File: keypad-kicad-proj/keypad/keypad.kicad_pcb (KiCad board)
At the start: 2 copper layers, 160 x 125 mm, 103 parts, among them J1 Screw_Terminal_01x02, J2 USB4105-GF-A, J3 USB4105-GF-A, J4 Micro_SD_Card_Det_Hirose_DM3AT, Q1 BC817, Q2 BC817, Q3 IRF9393TRPBF, SW1 RotaryEncoder, SW2 RotaryEncoder, SW25 SW_RST, SW26 Cherry_MX, SW27 Cherry_MX, SW28 Cherry_MX, SW32 Cherry_MX, SW33 Cherry_MX, SW34 Cherry_MX, SW38 Cherry_MX, SW39 Cherry_MX, SW40 Cherry_MX, SW44 Cherry_MX, SW45 Cherry_MX, SW46 Cherry_MX, U1 ESP32-S3-WROOM-1, U10 SK6812MINI-E, U11 SK6812MINI-E, U12 SK6812MINI-E, U13 SK6812MINI-E, U14 SK6812MINI-E, U2 TLV75901PDRVT, U27 SK6812MINI-E, U3 CP2102N-A01-GQFN24, U4 SK6812MINI-E, U5 SK6812MINI-E, U6 SK6812MINI-E, U7 SK6812MINI-E, U8 SK6812MINI-E, U9 SK6812MINI-E

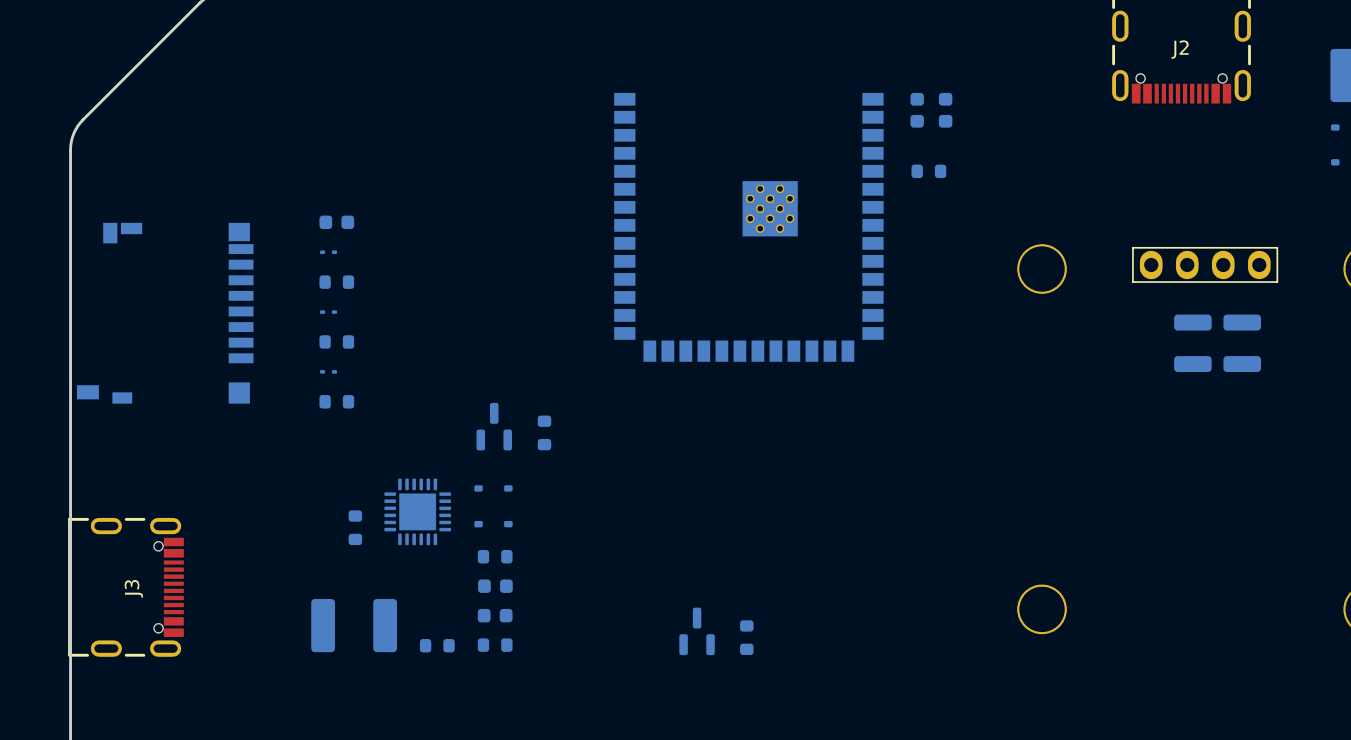
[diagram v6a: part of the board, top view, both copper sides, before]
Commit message: assigned different pins so it's easier for the layout
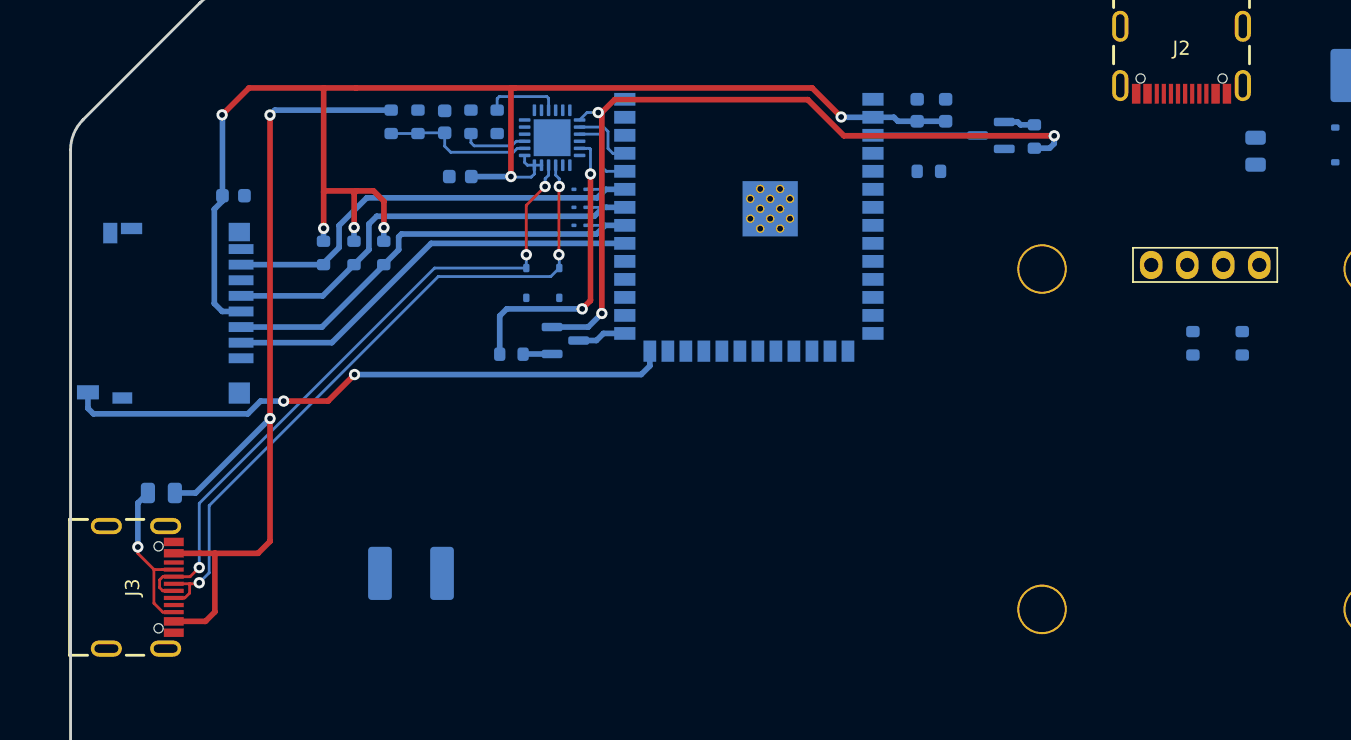
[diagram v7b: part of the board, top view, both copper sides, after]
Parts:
- added R22: 56k, Capacitor_SMD:C_0805_2012Metric, B.Cu at (55.9, 75.3)
- added R23: 56k, Capacitor_SMD:C_0805_2012Metric, B.Cu at (133.1, 51.2)
- R21, R6: footprint Resistor_SMD:R_1210_3225Metric -> Resistor_SMD:R_0603_1608Metric
- moved R10 40.7 mm to (117.5, 50.2), turned to -90 degrees
- moved Q1 40.6 mm to (114.4, 50.1), turned to 180 degrees
- moved R7 37.3 mm to (74.0, 49.1), turned to 90 degrees
- moved R5 37.1 mm to (72.1, 49.1), turned to -90 degrees
- moved C5 35.0 mm to (75.9, 49.1), turned to 90 degrees
- moved R9 30.7 mm to (77.7, 49.1), turned to 90 degrees
- moved R8 30.3 mm to (79.6, 49.1)
- moved C6 29.0 mm to (77.0, 53.0)
- moved U3 28.0 mm to (83.5, 50.3), turned to 90 degrees
- moved D25 20.5 mm to (85.4, 56.4), turned to 180 degrees
- moved D24 19.2 mm to (85.4, 55.2), turned to 180 degrees
- moved D23 18.3 mm to (85.4, 53.9), turned to 180 degrees
- moved D21 17.2 mm to (81.7, 60.5), turned to -90 degrees
- moved D19 15.2 mm to (84.0, 60.5), turned to -90 degrees
- moved R15 11.0 mm to (71.6, 58.4), turned to -90 degrees
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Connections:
- U1 pad 10: unconnected-(U1-IO17-Pad10) -> rotary_encoder_1B
- U1 pad 11: unconnected-(U1-IO18-Pad11) -> rotary_encoder_2B
- U1 pad 12: rotary_encoder_1A -> unconnected-(U1-IO8-Pad12)
- U1 pad 16: row_0 -> unconnected-(U1-IO46-Pad16)
- U1 pad 17: rotary_encoder_1B -> unconnected-(U1-IO9-Pad17)
- U1 pad 18: rotary_encoder_2A -> col_3
- U1 pad 19: rotary_encoder_2B -> col_2
- U1 pad 20: slide_potentiometer -> col_1
- U1 pad 22: col_1 -> row_2
- U1 pad 23: unconnected-(U1-IO21-Pad23) -> row_1
- U1 pad 24: unconnected-(U1-IO47-Pad24) -> row_0
- U1 pad 25: unconnected-(U1-IO48-Pad25) -> LED_strip
- U1 pad 28: row_1 -> unconnected-(U1-IO35-Pad28)
- U1 pad 29: row_2 -> unconnected-(U1-IO36-Pad29)
- U1 pad 5: LED_strip -> unconnected-(U1-IO5-Pad5)
- U1 pad 7: unconnected-(U1-IO7-Pad7) -> slide_potentiometer
- U1 pad 8: col_2 -> rotary_encoder_1A
- U1 pad 9: col_3 -> rotary_encoder_2A
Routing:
- net +3V3: track 0.00 -> 103.6 mm, vias 0 -> 6
- net USB-C_UART_VBUS: track 0.00 -> 62.1 mm, vias 0 -> 2
- net Net-(Q2-E): track 0.00 -> 55.0 mm, vias 0 -> 3
- net USB-C_UART_D+: track 0.00 -> 48.5 mm, vias 0 -> 3
- net USB-C_UART_D-: track 0.00 -> 47.2 mm, vias 0 -> 3
- net SD_DET: track 0.00 -> 43.3 mm, vias 0 -> 2
- net SD_CLK: track 0.00 -> 32.2 mm
- net SD_MOSI: track 0.00 -> 31.9 mm
- net SD_MISO: track 0.00 -> 31.7 mm
- net SD_CS: track 0.00 -> 30.0 mm
- net Net-(Q1-E): track 0.00 -> 21.0 mm, vias 0 -> 2
- net Net-(J3-CC1): track 0.00 -> 11.6 mm, vias 0 -> 1
- net Net-(U3-VBUS): track 0.00 -> 10.7 mm
- net RTS: track 0.00 -> 7.38 mm
- net UART_TX: track 0.00 -> 5.56 mm
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
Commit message: layout update
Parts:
- removed D1: LED, LED_SMD:LED_0805_2012Metric_Pad1.15x1.40mm_HandSolder
- removed R16: 2k, Resistor_SMD:R_0603_1608Metric
- moved D18 103.4 mm to (165.9, 34.6)
- moved R18 47.9 mm to (204.4, 99.8), turned to 0 degrees
- moved RV1 44.7 mm to (185.1, 101.3), turned to -90 degrees
- moved D27 44.3 mm to (199.3, 99.8), turned to 180 degrees
- moved R17 39.5 mm to (204.2, 95.6), turned to 0 degrees
- moved D26 35.3 mm to (199.3, 95.6), turned to 180 degrees
- moved R20 25.1 mm to (90.8, 68.8), turned to 0 degrees
- moved D17 17.0 mm to (155.2, 35.9)
- moved D16 16.1 mm to (145.7, 37.0), turned to 90 degrees
- moved Q3 15.9 mm to (199.3, 71.1)
- moved D22 15.6 mm to (200.7, 66.9)
- moved R2 14.8 mm to (192.9, 72.9), turned to 180 degrees
- moved R4 14.3 mm to (193.1, 70.9), turned to 0 degrees
- moved D15 12.8 mm to (140.6, 36.8), turned to 90 degrees
- moved R19 12.3 mm to (173.3, 76.1)
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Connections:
- U1 pad 10: rotary_encoder_1B -> rotary_encoder_2B
- U1 pad 11: rotary_encoder_2B -> rotary_encoder_2A
- U1 pad 16: unconnected-(U1-IO46-Pad16) -> rotary_encoder_1B
- U1 pad 17: unconnected-(U1-IO9-Pad17) -> rotary_encoder_1A
- U1 pad 4: indicator -> unconnected-(U1-IO4-Pad4)
- U1 pad 8: rotary_encoder_1A -> unconnected-(U1-IO15-Pad8)
- U1 pad 9: rotary_encoder_2A -> unconnected-(U1-IO16-Pad9)
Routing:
- net +5V: track 0.00 -> 371.0 mm, vias 0 -> 13
- net +3V3: track 103.6 -> 280.5 mm, vias 6 -> 9
- net row_2: track 0.00 -> 169.5 mm, vias 0 -> 3
- net row_1: track 0.00 -> 149.0 mm, vias 0 -> 1
- net rotary_encoder_1A: track 0.00 -> 138.0 mm
- net col_3: track 0.00 -> 133.6 mm
- net rotary_encoder_1B: track 0.00 -> 130.3 mm
- net row_0: track 0.00 -> 125.6 mm
- net slide_potentiometer: track 0.00 -> 120.9 mm, vias 0 -> 2
- net col_2: track 0.00 -> 116.4 mm, vias 0 -> 8
- net Net-(U7-DOUT): track 0.00 -> 114.6 mm
- net Net-(U11-DOUT): track 0.00 -> 114.5 mm
- net rotary_encoder_2A: track 0.00 -> 103.4 mm, vias 0 -> 2
- net col_0: track 0.00 -> 103.0 mm, vias 0 -> 8
- net rotary_encoder_2B: track 0.00 -> 97.7 mm, vias 0 -> 2
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- removed copper zone on B.Cu, net GND
- removed copper zone on F.Cu, net GND
